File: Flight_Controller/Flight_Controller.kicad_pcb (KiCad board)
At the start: 2 copper layers, 43.6 x 50 mm, 81 parts, among them IC1 AT7456E, J10 USB_C_Receptacle_USB2.0_16P, J11 Conn_ARM_SWD_TagConnect_TC203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, J13 SM06B-GHS-TB, J14 VTX, J6 ESC->FC DSHOT and Telem, J7 ELRS Reciever, J9 Camera, SW1 SW_Push, U1 STM32H743VITx, U2 BMI270, U3 TLV75533PDBV, U4 W25Q128JVSIQ TR, U6 LMR51625XDDCR, U7 TPD2EUSB30ADRTR, Y2 ABM3-27.000MHZ-D2Y-T

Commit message: Layout V2
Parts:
- removed D1: Red, PCM_JLCPCB:D_0603
- removed R9: 150Ω, PCM_JLCPCB:R_0603
- moved C17 15.4 mm to (99.8, 73.0), turned to 90 degrees
- moved C15 13.5 mm to (102.0, 73.8), turned to 0 degrees
- moved R13 10.8 mm to (94.9, 55.4)
- moved U3 7.53 mm to (100.8, 76.6), turned to 90 degrees
- moved C22 3.34 mm to (102.1, 63.7)
- moved D3 2.80 mm to (100.2, 87.6)
- moved C34 2.60 mm to (104.2, 81.0)
- moved C8 2.41 mm to (102.1, 60.7)
- moved R15 2.34 mm to (102.2, 87.6)
- moved C9 2.18 mm to (102.1, 62.2)
- moved H1 2.12 mm to (98.9, 52.1)
- moved H2 2.12 mm to (128.9, 52.1)
- moved H3 2.12 mm to (98.9, 82.1)
- moved H4 2.12 mm to (128.9, 82.1)
- moved C13 2.04 mm to (104.2, 78.8)
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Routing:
- net +5V: track 0.00 -> 22.9 mm
- net +BATT: track 0.00 -> 19.7 mm
- net +3V3: track 0.00 -> 7.77 mm
- net /Peripherals/Power/SW: track 0.00 -> 3.96 mm
- net /Peripherals/Power/LDO_LED: track 0.00 -> 2.00 mm
- net /Peripherals/Power/5V_LED: track 0.00 -> 2.00 mm
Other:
- board size 43.6 x 50 mm -> 42 x 46 mm
- copper layers 2 -> 4

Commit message: Updated Connector Standard
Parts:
- added D8: Red, PCM_JLCPCB:D_0603, F.Cu at (127.5, 77.7)
- added R19: 150Ω, PCM_JLCPCB:R_0603, F.Cu at (131.0, 77.7)
- J11: moved to B.Cu
- moved D5 12.6 mm to (101.2, 75.4), turned to 0 degrees
- moved R17 11.0 mm to (99.6, 77.1), turned to 0 degrees
- moved J11 11.0 mm to (123.7, 54.4), turned to 90 degrees
- moved C13 6.18 mm to (104.5, 85.0)
- moved C14 4.88 mm to (104.7, 88.6), turned to 180 degrees
- moved R16 4.80 mm to (127.7, 87.5), turned to 0 degrees
- moved U3 4.79 mm to (104.5, 79.5)
- moved D3 4.48 mm to (104.7, 87.0), turned to 0 degrees
- moved C15 4.01 mm to (102.0, 77.8), turned to -90 degrees
- moved R8 3.94 mm to (107.5, 78.8), turned to 90 degrees
- moved R14 3.92 mm to (98.1, 46.5)
- moved C27 3.86 mm to (100.8, 47.5)
- moved SW1 3.82 mm to (100.7, 45.6)
- moved C33 3.09 mm to (124.1, 85.1), turned to 0 degrees
- moved D4 3.08 mm to (124.1, 87.5), turned to 180 degrees
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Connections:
- J6 pad 7: +BATT -> GND
- J6 pad 8: GND -> +BATT
- U1 pad 46: unconnected-(U1-PB10-Pad46) -> /MCU/Connectors/PB10
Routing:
- net +5V: track 22.9 -> 0.00 mm
- net +BATT: track 19.7 -> 0.00 mm
- net +3V3: track 7.77 -> 0.00 mm
- net /Peripherals/Power/SW: track 3.96 -> 0.00 mm
- net /Peripherals/Power/LDO_LED: track 2.00 -> 0.00 mm
- net /Peripherals/Power/5V_LED: track 2.00 -> 0.00 mm
- added copper zone on F.Cu, net +3V3
- added copper zone on F.Cu, net +5V
- added copper zone on F.Cu, net +BATT
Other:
- outline, holes or cut-outs redrawn

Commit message: Updated Footprints
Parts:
- removed J14: VTX, Connector_JST:JST_GH_SM06B-GHS-TB_1x06-1MP_P1.25mm_Horizontal
- removed J6: ESC->FC DSHOT and Telem, Connector_JST:JST_GH_SM08B-GHS-TB_1x08-1MP_P1.25mm_Horizontal
- added C10: 100nF, PCM_JLCPCB:C_0603, F.Cu at (77.2, 85.6)
- added C12: 100nF, PCM_JLCPCB:C_0603, F.Cu at (77.2, 87.8)
- added C13: 22uF, PCM_JLCPCB:C_1206, F.Cu at (63.2, 76.0)
- added C34: 22uF, PCM_JLCPCB:C_1206, F.Cu at (63.2, 79.3)
- added C35: 22uF, PCM_JLCPCB:C_1206, F.Cu at (63.2, 82.7)
- added C36: 22uF, PCM_JLCPCB:C_1206, F.Cu at (63.2, 86.0)
- added C37: 22uF, PCM_JLCPCB:C_1206, F.Cu at (63.2, 89.4)
- added C5: 2.2uF, PCM_JLCPCB:C_0805, F.Cu at (71.9, 90.2)
- added D10: White, PCM_JLCPCB:D_0603, F.Cu at (77.3, 90.3)
- added J1: Analog VTX, Connector_JST:JST_SH_SM05B-SRSS-TB_1x05-1MP_P1.00mm_Horizontal, F.Cu at (96.2, 63.0)
- added J2: Digital VTX, Connector_JST:JST_SH_SM06B-SRSS-TB_1x06-1MP_P1.00mm_Horizontal, F.Cu at (77.2, 64.4)
- added J3: GPS+Mag, Connector_JST:JST_SH_SM06B-SRSS-TB_1x06-1MP_P1.00mm_Horizontal, F.Cu at (65.8, 68.5)
- added J4: ESC Connector, Connector_JST:JST_SH_SM10B-SRSS-TB_1x10-1MP_P1.00mm_Horizontal, F.Cu at (113.9, 87.3)
- added L2: 18uH, Inductor_SMD:L_TDK_VLP8040, F.Cu at (80.8, 79.4)
- added R14: 10kΩ, PCM_JLCPCB:R_0603, F.Cu at (67.8, 87.8)
- added R18: 820Ω, PCM_JLCPCB:R_0603, F.Cu at (67.8, 90.1)
- added R9: 100kΩ, PCM_JLCPCB:R_0603, F.Cu at (67.8, 85.6)
- added U8: LMR51625XDDCR, Flight_Controller:DDC0006A-MFG, F.Cu at (72.9, 86.6)
- J7: footprint Connector_JST:JST_GH_SM04B-GHS-TB_1x04-1MP_P1.25mm_Horizontal -> Connector_JST:JST_SH_SM04B-SRSS-TB_1x04-1MP_P1.00mm_Horizontal
- J9: footprint Connector_JST:JST_GH_SM03B-GHS-TB_1x03-1MP_P1.25mm_Horizontal -> Connector_JST:JST_SH_SM03B-SRSS-TB_1x03-1MP_P1.00mm_Horizontal
- SW1: footprint Resistor_SMD:R_0805_2012Metric -> Flight_Controller:SW_TS-1088-AR02016
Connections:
- C1 pad 2: /Peripherals/Power/<NO NET> -> /MCU/Connectors/VIDEO_IN
- J7 pad 2: /MCU/Connectors/ELRS_RX -> GND
- J7 pad 3: /MCU/Connectors/ELRS_TX -> /MCU/Connectors/ELRS_RX
- J7 pad 4: GND -> /MCU/Connectors/ELRS_TX
- J9 pad 2: /Peripherals/Power/<NO NET> -> GND
- J9 pad 3: GND -> /MCU/Connectors/VIDEO_IN
- R4 pad 1: /Peripherals/Power/<NO NET> -> /MCU/Connectors/VIDEO_IN
- SW1 pad 1: /MCU/Connectors/RST_SW -> GND
- U1 pad 37: unconnected-(U1-PE7-Pad37) -> /MCU/Connectors/DVTX_RX
- U1 pad 38: unconnected-(U1-PE8-Pad38) -> /MCU/Connectors/DVTX_TX
- U1 pad 59: unconnected-(U1-PD12-Pad59) -> /MCU/Connectors/Mag_SCL
- U1 pad 60: unconnected-(U1-PD13-Pad60) -> /MCU/Connectors/Mag_SDA
- U1 pad 61: unconnected-(U1-PD14-Pad61) -> /MCU/Connectors/M5_DSHOT
- U1 pad 62: unconnected-(U1-PD15-Pad62) -> /MCU/Connectors/M6_DSHOT
- U1 pad 64: unconnected-(U1-PC7-Pad64) -> /MCU/Connectors/SBUS
- U1 pad 91: unconnected-(U1-PB5-Pad91) -> /MCU/Connectors/GPS_TX
- U1 pad 92: unconnected-(U1-PB6-Pad92) -> /MCU/Connectors/GPS_RX

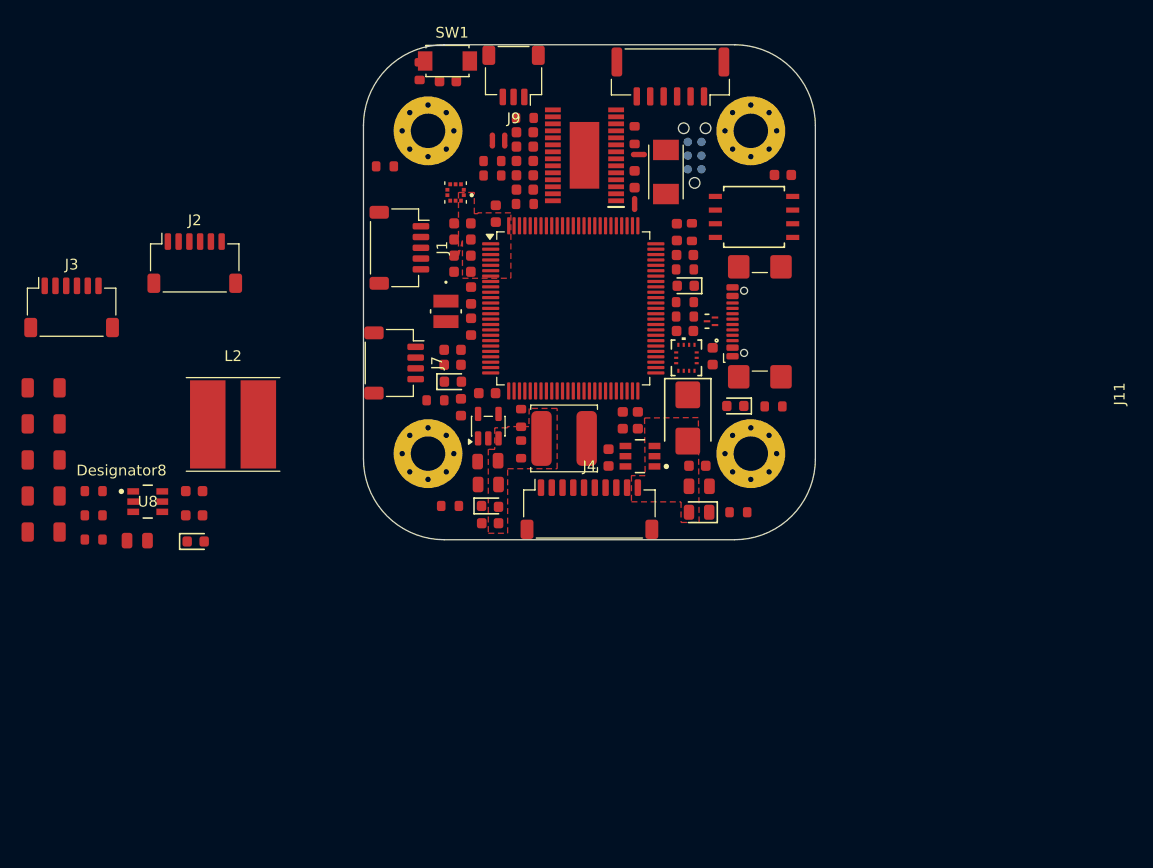
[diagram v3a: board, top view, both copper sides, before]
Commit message: Updated Layout to 60x30
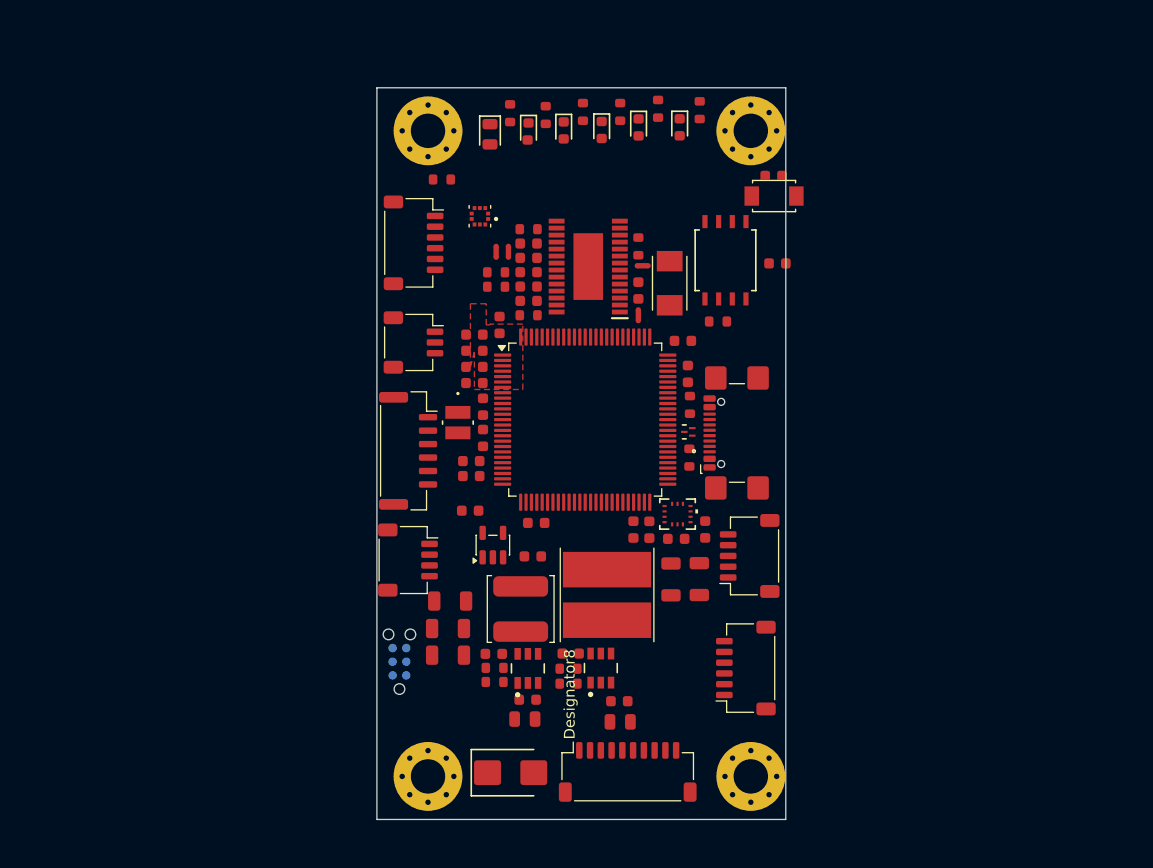
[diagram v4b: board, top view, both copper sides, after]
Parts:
- removed the C13 at (104.5, 85.0)
- removed the C34 at (104.5, 82.8)
- removed the R14 at (98.1, 46.5)
- moved J2 63.6 mm to (128.4, 102.0), turned to 90 degrees
- moved C36 61.4 mm to (124.1, 93.8), turned to -90 degrees
- moved R18 60.4 mm to (113.3, 50.3), turned to 90 degrees
- moved C37 58.5 mm to (121.5, 93.8), turned to -90 degrees
- moved J11 54.5 mm to (96.2, 101.4)
- moved D10 51.3 mm to (111.5, 52.1), turned to -90 degrees
- moved C5 47.9 mm to (116.8, 107.0)
- moved R9 47.1 mm to (112.0, 102.1)
- moved R14 46.8 mm to (112.0, 103.5), turned to 180 degrees
- moved U8 44.9 mm to (115.0, 102.0), turned to 90 degrees
- moved C10 44.1 mm to (116.7, 105.1)
- moved C13 43.7 mm to (100.8, 98.4), turned to 180 degrees
- moved J1 43.4 mm to (128.8, 91.6), turned to 90 degrees
- moved C34 43.3 mm to (100.8, 100.8), turned to 180 degrees
- moved R16 42.7 mm to (106.5, 50.5), turned to 90 degrees
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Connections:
- net /MCU/Connectors/3V3_LED renamed /MCU/Connectors/MCU_LED
- C11 pad 1: /Peripherals/Power/CB -> /Peripherals/Power/CB_5V
- C11 pad 2: /Peripherals/Power/SW -> /Peripherals/Power/SW_5V
- C12 pad 1: /Peripherals/Power/CB -> /Peripherals/Power/CB_9V
- C12 pad 2: /Peripherals/Power/SW -> /Peripherals/Power/SW_9V
- L1 pad 1: /Peripherals/Power/SW -> /Peripherals/Power/SW_5V
- L2 pad 1: /Peripherals/Power/SW -> /Peripherals/Power/SW_9V
- R14 pad 1: /Peripherals/Power/FB -> /Peripherals/Power/FB_9V
- R7 pad 2: /Peripherals/Power/FB -> /Peripherals/Power/FB_5V
- R8 pad 1: /Peripherals/Power/FB -> /Peripherals/Power/FB_5V
- R9 pad 2: /Peripherals/Power/FB -> /Peripherals/Power/FB_9V
- U6 pad 1: /Peripherals/Power/FB -> /Peripherals/Power/FB_5V
- U6 pad 5: /Peripherals/Power/SW -> /Peripherals/Power/SW_5V
- U6 pad 6: /Peripherals/Power/CB -> /Peripherals/Power/CB_5V
- U8 pad 1: /Peripherals/Power/FB -> /Peripherals/Power/FB_9V
- U8 pad 5: /Peripherals/Power/SW -> /Peripherals/Power/SW_9V
- U8 pad 6: /Peripherals/Power/CB -> /Peripherals/Power/CB_9V
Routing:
- removed copper zone on F.Cu, net +5V
- removed copper zone on F.Cu, net +BATT
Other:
- board size 42 x 46 mm -> 38 x 68 mm

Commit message: More Layout Updates
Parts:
- moved R13 8.55 mm to (103.7, 48.8)
- moved J11 4.79 mm to (99.0, 105.4), turned to 180 degrees
- moved J9 2.01 mm to (98.0, 69.8)
- moved J13 1.80 mm to (97.0, 80.0)
- moved J3 1.74 mm to (98.2, 60.9)
- moved C35 0.52 mm to (101.5, 95.8)
- moved C13 0.52 mm to (101.3, 98.4)
- moved C34 0.52 mm to (101.3, 100.8)
- moved C28 0.29 mm to (123.3, 74.7)
- moved R11 0.29 mm to (123.5, 82.5)
- moved R12 0.29 mm to (123.5, 77.6)
- moved U7 0.29 mm to (123.4, 80.1)
- moved J10 0.29 mm to (129.0, 80.2)
- moved XTAL1 0.16 mm to (101.8, 79.2)
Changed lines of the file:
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@@
 		(capping no)
 		(filling no)
-		(grid_origin 113.9 67.1)
+		(grid_origin 113.9 82.1)
 		(pcbplotparams
 			(layerselection 0x00000000_00000000_55555555_5755f5ff)
@@
 	(footprint "Connector_USB:USB_C_Receptacle_GCT_USB4110"
 		(layer "F.Cu")
-		(at 128.75 80.18 90)
+		(at 129.04 80.18 90)
 		(descr "USB 2.0 Type C Receptacle, GCT, 16P, top mounted, horizontal, 5A, https://gct.co/files/drawings/usb4110.pdf")
 		(tags "USB 2.0 C Type-C Receptacle SMD 16P 16C USB4110-GF-A")
@@
 	(footprint "PCM_JLCPCB:R_0603"
 		(layer "F.Cu")
-		(at 123.24 77.57 -90)
+		(at 123.53 77.57 -90)
 		(descr "Resistor SMD 0603 (1608 Metric), square (rectangular) end terminal, IPC_7351 nominal, (Body size source: IPC-SM-782 page 72, https://www.pcb-3d.com/wordpress/wp-content/uploads/ipc-sm-782a_amendment_1_and_2.pdf), generated with kicad-footprint-generator")
 		(tags "resistor")
@@
 	(footprint "Connector_JST:JST_SH_SM06B-SRSS-TB_1x06-1MP_P1.00mm_Horizontal"
 		(layer "F.Cu")
-		(at 97.56 62.51 -90)
+		(at 98.175 60.88 -90)
 		(descr "JST SH series connector, SM06B-SRSS-TB (http://www.jst-mfg.com/product/pdf/eng/eSH.pdf)")
 		(tags "connector JST SH horizontal")
@@
 	(footprint "Flight_Controller:DRT3-L"
 		(layer "F.Cu")
-		(at 123.0899 80.08 90)
+		(at 123.3799 80.08 90)
 		(tags "TPD2EUSB30ADRTR ")
 		(property "Reference" "U7"
@@
 	(footprint "Flight_Controller:XTAL_NX3225GD-8MHZ-STD-CRA-3_NDK-L"
 		(layer "F.Cu")
-		(at 101.675 79.218 -90)
+		(at 101.83 79.218 -90)
 		(tags "NX3225GD-8MHZ-STD-CRA-3 ")
 		(property "Reference" "XTAL1"
@@
 	(footprint "PCM_JLCPCB:R_0603"
 		(layer "F.Cu")
-		(at 123.19 82.47 90)
+		(at 123.48 82.47 90)
 		(descr "Resistor SMD 0603 (1608 Metric), square (rectangular) end terminal, IPC_7351 nominal, (Body size source: IPC-SM-782 page 72, https://www.pcb-3d.com/wordpress/wp-content/uploads/ipc-sm-782a_amendment_1_and_2.pdf), generated with kicad-footprint-generator")
 		(tags "resistor")
@@
 	(footprint "PCM_JLCPCB:R_0603"
 		(layer "F.Cu")
-		(at 100.19 56.62)
+		(at 103.7 48.82)
 		(descr "Resistor SMD 0603 (1608 Metric), square (rectangular) end terminal, IPC_7351 nominal, (Body size source: IPC-SM-782 page 72, https://www.pcb-3d.com/wordpress/wp-content/uploads/ipc-sm-782a_amendment_1_and_2.pdf), generated with kicad-footprint-generator")
 		(tags "resistor")
@@
 	(footprint "PCM_JLCPCB:C_1206"
 		(layer "F.Cu")
-		(at 100.76 98.356926 180)
+		(at 101.28 98.356926 180)
 		(descr "Capacitor SMD 1206 (3216 Metric), square (rectangular) end terminal, IPC_7351 nominal, (Body size source: IPC-SM-782 page 76, https://www.pcb-3d.com/wordpress/wp-content/uploads/ipc-sm-782a_amendment_1_and_2.pdf), generated with kicad-footprint-generator")
 		(tags "capacitor")
@@
 	(footprint "PCM_JLCPCB:C_1206"
 		(layer "F.Cu")
-		(at 100.76 100.83 180)
+		(at 101.28 100.83 180)
 		(descr "Capacitor SMD 1206 (3216 Metric), square (rectangular) end terminal, IPC_7351 nominal, (Body size source: IPC-SM-782 page 76, https://www.pcb-3d.com/wordpress/wp-content/uploads/ipc-sm-782a_amendment_1_and_2.pdf), generated with kicad-footprint-generator")
 		(tags "capacitor")
@@
 	(footprint "Connector_JST:JST_GH_SM06B-GHS-TB_1x06-1MP_P1.25mm_Horizontal"
 		(layer "F.Cu")
-		(at 97.05 81.84 -90)
+		(at 97.05 80.045 -90)
 		(descr "JST GH series connector, SM06B-GHS-TB (http://www.jst-mfg.com/product/pdf/eng/eGH.pdf)")
 		(tags "connector JST GH horizontal")
@@
 	(footprint "PCM_JLCPCB:C_0603"
 		(layer "F.Cu")
-		(at 123.05 74.69 -90)
+		(at 123.34 74.69 -90)
 		(descr "Capacitor SMD 0603 (1608 Metric), square (rectangular) end terminal, IPC_7351 nominal, (Body size source: IPC-SM-782 page 76, https://www.pcb-3d.com/wordpress/wp-content/uploads/ipc-sm-782a_amendment_1_and_2.pdf), generated with kicad-footprint-generator")
 		(tags "capacitor")
@@
 	(footprint "Connector_JST:JST_SH_SM03B-SRSS-TB_1x03-1MP_P1.00mm_Horizontal"
 		(layer "F.Cu")
-		(at 97.55 71.77 -90)
+		(at 98.03 69.82 -90)
 		(descr "JST SH series connector, SM03B-SRSS-TB (http://www.jst-mfg.com/product/pdf/eng/eSH.pdf)")
 		(tags "connector JST SH horizontal")
@@
 	(footprint "PCM_JLCPCB:C_1206"
 		(layer "F.Cu")
-		(at 100.96 95.8 180)
+		(at 101.48 95.8 180)
 		(descr "Capacitor SMD 1206 (3216 Metric), square (rectangular) end terminal, IPC_7351 nominal, (Body size source: IPC-SM-782 page 76, https://www.pcb-3d.com/wordpress/wp-content/uploads/ipc-sm-782a_amendment_1_and_2.pdf), generated with kicad-footprint-generator")
 		(tags "capacitor")
@@
 	(footprint "Connector:Tag-Connect_TC2030-IDC-NL_2x03_P1.27mm_Vertical"
 		(layer "B.Cu")
-		(at 96.245 101.44 90)
+		(at 98.99 105.36 180)
 		(descr "Tag-Connect programming header; http://www.tag-connect.com/Materials/TC2030-IDC-NL.pdf")
 		(tags "tag connect programming header pogo pins")
 		(property "Reference" "J11"
-			(at -22.153 39.497 90)
+			(at -22.153 39.497 0)
 			(layer "F.SilkS")
 			(hide yes)
@@
 		)
 		(property "Value" "Conn_ARM_SWD_TagConnect_TC2030-NL"
-			(at 19.5571 36.483 90)
+			(at 19.5571 36.483 0)
 			(layer "F.Fab")
 			(hide yes)
@@
 		)
 		(property "Datasheet" "https://www.tag-connect.com/wp-content/uploads/bsk-pdf-manager/TC2030-CTX_1.pdf"
-			(at 0 0 270)
+			(at 0 0 0)
 			(unlocked yes)
 			(layer "B.Fab")
@@
 		)
 		(property "Description" "Tag-Connect ARM Cortex SWD JTAG connector, 6 pin, no legs"
-			(at 0 0 270)
+			(at 0 0 0)
 			(unlocked yes)
 			(layer "B.Fab")
@@
 		)
 		(fp_line
-			(start 3.5 -2)
-			(end -3.5 -2)
+			(start 3.5 2)
+			(end 3.5 -2)
 			(stroke
 				(width 0.05)
@@
 		)
 		(fp_line
-			(start -3.5 -2)
-			(end -3.5 2)
+			(start 3.5 -2)
+			(end -3.5 -2)
 			(stroke
 				(width 0.05)
@@
 		)
 		(fp_line
-			(start 3.5 2)
-			(end 3.5 -2)
+			(start -3.5 2)
+			(end 3.5 2)
 			(stroke
 				(width 0.05)
@@
 		)
 		(fp_line
-			(start -3.5 2)
-			(end 3.5 2)
+			(start -3.5 -2)
+			(end -3.5 2)
 			(stroke
 				(width 0.05)
@@
 		)
 		(fp_text user "KEEPOUT"
-			(at -22.153 36.797 90)
+			(at -22.153 36.797 0)
 			(layer "Cmts.User")
 			(effects
@@
 		)
 		(fp_text user "${REFERENCE}"
-			(at -22.153 36.797 90)
+			(at -22.153 36.797 0)
 			(layer "F.Fab")
 			(effects
@@
 		)
 		(pad "" np_thru_hole circle
-			(at -2.54 0 90)
+			(at -2.54 0 180)
 			(size 0.9906 0.9906)
 			(drill 0.9906)
@@
 		)
 		(pad "" np_thru_hole circle
-			(at 2.54 -1.016 90)
+			(at 2.54 -1.016 180)
 			(size 0.9906 0.9906)
 			(drill 0.9906)
@@
 		)
 		(pad "" np_thru_hole circle
-			(at 2.54 1.016 90)
+			(at 2.54 1.016 180)
 			(size 0.9906 0.9906)
 			(drill 0.9906)
@@
 		)
 		(pad "1" connect circle
-			(at -1.27 -0.635 90)
+			(at -1.27 -0.635 180)
 			(size 0.7874 0.7874)
 			(layers "B.Cu" "B.Mask")
@@
 		)
 		(pad "2" connect circle
-			(at -1.27 0.635 90)
+			(at -1.27 0.635 180)
 			(size 0.7874 0.7874)
 			(layers "B.Cu" "B.Mask")
@@
 		)
 		(pad "3" connect circle
-			(at 0 -0.635 90)
+			(at 0 -0.635 180)
 			(size 0.7874 0.7874)
 			(layers "B.Cu" "B.Mask")
@@
 		)
 		(pad "4" connect circle
-			(at 0 0.635 90)
+			(at 0 0.635 180)
 			(size 0.7874 0.7874)
 			(layers "B.Cu" "B.Mask")
@@
 		)
 		(pad "5" connect circle
-			(at 1.27 -0.635 90)
+			(at 1.27 -0.635 180)
 			(size 0.7874 0.7874)
 			(layers "B.Cu" "B.Mask")
@@
 		)
 		(pad "6" connect circle
-			(at 1.27 0.635 90)
+			(at 1.27 0.635 180)
 			(size 0.7874 0.7874)
 			(layers "B.Cu" "B.Mask")
@@
 			(polygon
 				(pts
-					(xy 96.88 100.17) (xy 96.88 102.71) (xy 95.61 102.71) (xy 95.61 100.17)
+					(xy 97.72 104.725) (xy 100.26 104.725) (xy 100.26 105.995) (xy 97.72 105.995)
 				)
 			)
@@
 	)
 	(gr_rect
-		(start 94.15 48.1)
-		(end 132.15 116.1)
+		(start 94.9 48.1)
+		(end 132.9 116.1)
 		(stroke
 			(width 0.05)

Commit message: Almost Done Routing!
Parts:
- R13: moved to B.Cu
- moved R13 25.5 mm to (109.2, 73.7)
- moved A1 10.7 mm to (103.2, 70.7)
- moved SW1 10.4 mm to (140.0, 52.7)
- moved C27 7.70 mm to (138.7, 55.5)
- moved C4 5.79 mm to (128.1, 69.2), turned to 0 degrees
- moved R3 1.94 mm to (118.4, 60.9), turned to -90 degrees
- moved C8 1.91 mm to (104.9, 70.1), turned to 90 degrees
- moved J7 1.74 mm to (98.1, 90.6)
- moved C26 1.72 mm to (103.1, 82.1), turned to 0 degrees
- moved C25 1.27 mm to (103.0, 77.0), turned to 0 degrees
- moved XTAL1 1.19 mm to (103.0, 79.6)
- moved C20 1.18 mm to (121.6, 71.0), turned to 90 degrees
- moved J2 1.09 mm to (129.5, 102.0)
- moved J13 1.08 mm to (98.1, 79.8)
- moved R6 0.90 mm to (125.2, 69.2)
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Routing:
- net +BATT: track 0.00 -> 59.1 mm, vias 0 -> 2
- net /MCU/Connectors/SWCLK: track 0.00 -> 55.7 mm, vias 0 -> 4
- net /MCU/Connectors/VIDEO_OUT: track 0.00 -> 55.5 mm, vias 0 -> 3
- net /MCU/Connectors/SWDIO: track 0.00 -> 51.9 mm, vias 0 -> 4
- net /MCU/Connectors/SWO: track 0.00 -> 49.3 mm, vias 0 -> 4
- net /MCU/Connectors/Mag_SCL: track 0.00 -> 42.5 mm, vias 0 -> 3
- net /MCU/Connectors/Mag_SDA: track 0.00 -> 40.5 mm, vias 0 -> 3
- net /MCU/Connectors/NRST: track 0.00 -> 38.7 mm, vias 0 -> 3
- net /MCU/Connectors/M1_DSHOT: track 0.00 -> 38.6 mm, vias 0 -> 3
- net /MCU/Connectors/ADC_CURR: track 0.00 -> 38.5 mm, vias 0 -> 3
- net +5V: track 0.00 -> 36.9 mm, vias 0 -> 1
- net /MCU/Connectors/M2_DSHOT: track 0.00 -> 35.4 mm, vias 0 -> 3
- net /MCU/Connectors/M3_DSHOT: track 0.00 -> 34.9 mm, vias 0 -> 3
- net /MCU/Connectors/M4_DSHOT: track 0.00 -> 33.9 mm, vias 0 -> 3
- net +3V3: track 0.00 -> 33.1 mm, vias 0 -> 5
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- added copper zone on F.Cu, net +5V
- added copper zone on F.Cu, net +9V
- added copper zone on F.Cu, net +BATT
- added copper zone on F.Cu, net /MCU/Connectors/BB_SPI_CS
- added copper zone on F.Cu, net /MCU/Connectors/OSC_IN
- added copper zone on F.Cu, net /MCU/Connectors/OSC_OUT
- added copper zone on F.Cu, net /MCU/Connectors/OSD_LOS
- added copper zone on F.Cu, net /MCU/Connectors/OSD_VS
- added copper zone on F.Cu, net /Peripherals/Power/FB_5V
- added copper zone on F.Cu, net /Peripherals/Power/FB_9V
- added copper zone on F.Cu, net /Peripherals/Power/SW_5V
- added copper zone on F.Cu, net /Peripherals/Power/SW_9V
- added copper zone on F.Cu, net /Peripherals/Power/VOUT_RES
- added copper zone on F.Cu, net GND
